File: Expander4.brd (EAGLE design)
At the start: 160 x 100 mm, 6 parts, among them K1 G5L, K2 G5L, K3 G5L, K4 G5L

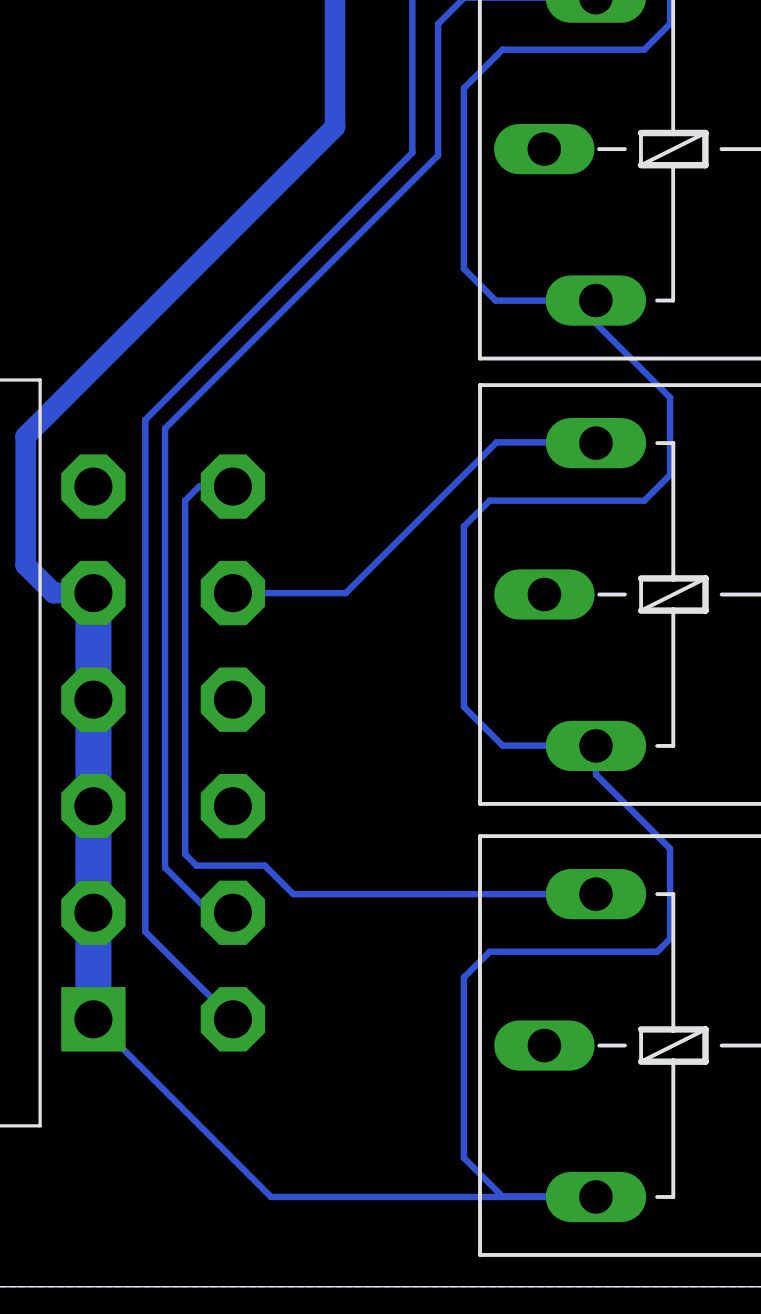
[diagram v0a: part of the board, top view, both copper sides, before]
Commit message: Protective diodes added in expander
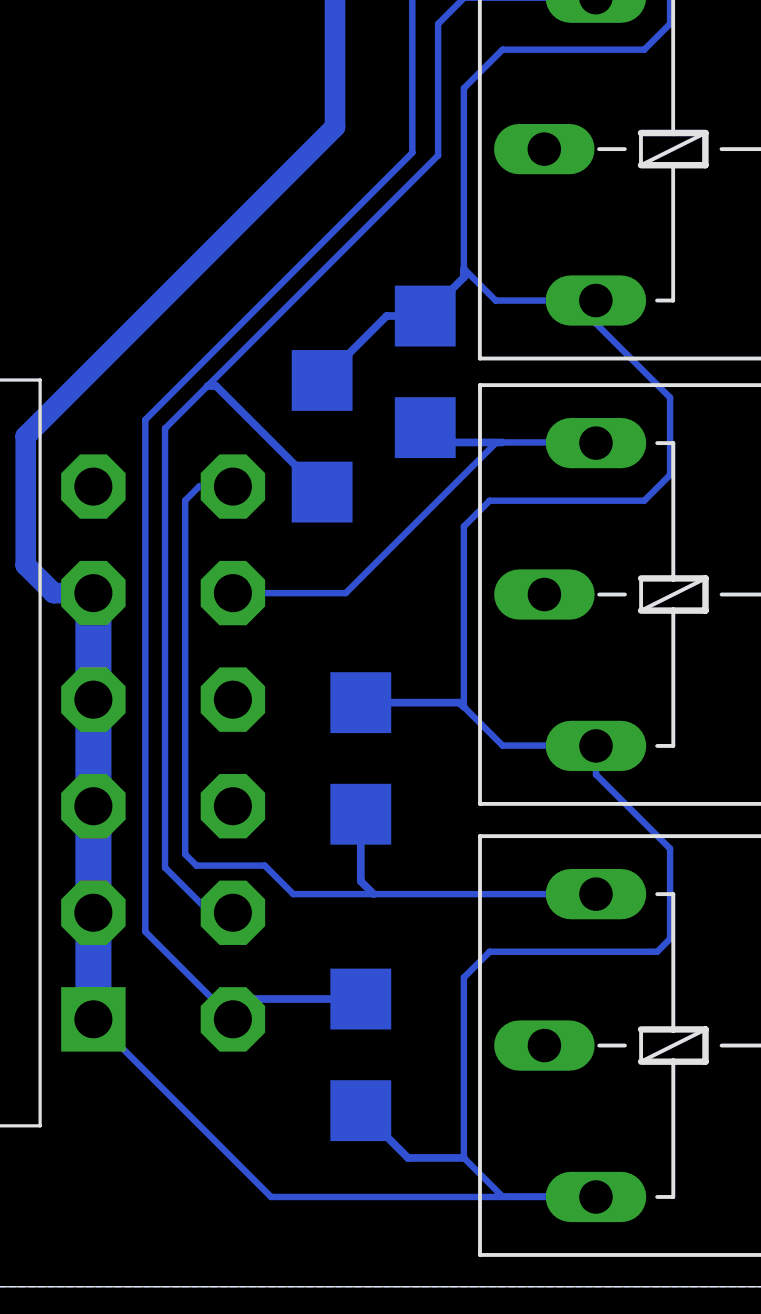
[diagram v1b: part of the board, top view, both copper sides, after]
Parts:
- added D1, D2, D3, D4: (no value), SparkFun-DiscreteSemi:SMB-DIODE
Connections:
- net 12V: now also D1.C, D2.C, D3.C, D4.C
- net L1: now also D2.A
- net L2: now also D1.A
- net L3: now also D3.A
- net L4: now also D4.A
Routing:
- net 12V: track 255.9 -> 272.5 mm
- net L3: track 47.8 -> 54.0 mm
- net L4: track 66.8 -> 72.2 mm
- net L1: track 32.9 -> 36.3 mm
- net L2: track 16.8 -> 20.1 mm
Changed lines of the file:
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@@
 </element>
 <element name="OUT" library="con-amphenol" package="MF42-10" value="MF42-10" x="53.634" y="14.738" rot="R90"/>
+<element name="D1" library="SparkFun-DiscreteSemi" package="SMB-DIODE" value="" x="18.796" y="36.068" rot="MR270"/>
+<element name="D2" library="SparkFun-DiscreteSemi" package="SMB-DIODE" value="" x="16.256" y="20.828" rot="MR270"/>
+<element name="D3" library="SparkFun-DiscreteSemi" package="SMB-DIODE" value="" x="14.732" y="33.528" rot="MR270"/>
+<element name="D4" library="SparkFun-DiscreteSemi" package="SMB-DIODE" value="" x="16.256" y="9.144" rot="MR90"/>
 </elements>
 <signals>
@@
 <wire x1="4.151" y1="27.345" x2="5.715" y2="27.345" width="0.8128" layer="16"/>
 <wire x1="28.448" y1="71.12" x2="23.876" y2="71.12" width="0.8128" layer="16"/>
+<contactref element="D1" pad="C"/>
+<contactref element="D2" pad="C"/>
+<contactref element="D3" pad="C"/>
+<contactref element="D4" pad="C"/>
+<wire x1="14.732" y1="35.728" x2="17.272" y2="38.268" width="0.3048" layer="16"/>
+<wire x1="17.272" y1="38.268" x2="18.796" y2="38.268" width="0.3048" layer="16"/>
+<wire x1="18.796" y1="38.268" x2="20.32" y2="39.792" width="0.3048" layer="16"/>
+<wire x1="20.32" y1="39.792" x2="20.32" y2="40.132" width="0.3048" layer="16"/>
+<wire x1="16.256" y1="23.028" x2="20.152" y2="23.028" width="0.3048" layer="16"/>
+<wire x1="20.152" y1="23.028" x2="20.32" y2="22.86" width="0.3048" layer="16"/>
+<wire x1="20.32" y1="5.08" x2="18.12" y2="5.08" width="0.3048" layer="16"/>
+<wire x1="18.12" y1="5.08" x2="16.256" y2="6.944" width="0.3048" layer="16"/>
 </signal>
 <signal name="GND">
@@
 <contactref element="IN" pad="12"/>
 <contactref element="K1" pad="2"/>
-<wire x1="25.527" y1="15.479" x2="13.59638125" y2="15.479" width="0.254" layer="16"/>
+<wire x1="25.527" y1="15.479" x2="16.764" y2="15.479" width="0.254" layer="16"/>
+<wire x1="16.764" y1="15.479" x2="13.59638125" y2="15.479" width="0.254" layer="16"/>
 <wire x1="13.59638125" y1="15.479" x2="12.4714" y2="16.60398125" width="0.254" layer="16"/>
 <wire x1="12.4714" y1="16.60398125" x2="9.778996875" y2="16.60398125" width="0.254" layer="16"/>
@@
 <wire x1="9.331959375" y1="30.99561875" x2="9.881340625" y2="31.545" width="0.254" layer="16"/>
 <wire x1="9.881340625" y1="31.545" x2="11.215" y2="31.545" width="0.254" layer="16"/>
+<contactref element="D2" pad="A"/>
+<wire x1="16.256" y1="18.628" x2="16.256" y2="15.987" width="0.3048" layer="16"/>
+<wire x1="16.256" y1="15.987" x2="16.764" y2="15.479" width="0.3048" layer="16"/>
 </signal>
 <signal name="L2">
 <contactref element="IN" pad="11"/>
 <contactref element="K2" pad="2"/>
-<wire x1="21.600159375" y1="33.284159375" x2="25.501840625" y2="33.284159375" width="0.254" layer="16"/>
+<wire x1="21.600159375" y1="33.284159375" x2="21.844" y2="33.284159375" width="0.254" layer="16"/>
+<wire x1="21.844" y1="33.284159375" x2="25.501840625" y2="33.284159375" width="0.254" layer="16"/>
 <wire x1="25.501840625" y1="33.284159375" x2="25.527" y2="33.259" width="0.254" layer="16"/>
 <wire x1="21.600159375" y1="33.284159375" x2="15.661" y2="27.345" width="0.254" layer="16"/>
 <wire x1="15.661" y1="27.345" x2="11.215" y2="27.345" width="0.254" layer="16"/>
+<contactref element="D1" pad="A"/>
+<wire x1="18.796" y1="33.868" x2="19.379840625" y2="33.284159375" width="0.3048" layer="16"/>
+<wire x1="19.379840625" y1="33.284159375" x2="21.844" y2="33.284159375" width="0.3048" layer="16"/>
 </signal>
 <signal name="L3">
@@
 <wire x1="8.53948125" y1="33.83448125" x2="8.53948125" y2="16.5227" width="0.254" layer="16"/>
 <wire x1="20.337" y1="50.817" x2="25.522" y2="50.817" width="0.254" layer="16"/>
-<wire x1="8.53948125" y1="33.83448125" x2="19.304" y2="44.599" width="0.254" layer="16"/>
+<wire x1="8.53948125" y1="33.83448125" x2="10.2125" y2="35.5075" width="0.254" layer="16"/>
+<wire x1="10.2125" y1="35.5075" x2="19.304" y2="44.599" width="0.254" layer="16"/>
 <wire x1="19.304" y1="44.599" x2="19.304" y2="49.784" width="0.254" layer="16"/>
 <wire x1="19.304" y1="49.784" x2="20.337" y2="50.817" width="0.254" layer="16"/>
+<contactref element="D3" pad="A"/>
+<wire x1="14.732" y1="31.328" x2="10.5525" y2="35.5075" width="0.3048" layer="16"/>
+<wire x1="10.5525" y1="35.5075" x2="10.2125" y2="35.5075" width="0.3048" layer="16"/>
 </signal>
 <signal name="L4">
@@
 <wire x1="18.288" y1="61.468" x2="25.321" y2="68.501" width="0.254" layer="16"/>
 <wire x1="25.321" y1="68.501" x2="25.501" y2="68.501" width="0.254" layer="16"/>
+<contactref element="D4" pad="A"/>
+<wire x1="16.256" y1="11.344" x2="12.014" y2="11.344" width="0.3048" layer="16"/>
+<wire x1="12.014" y1="11.344" x2="11.215" y2="10.545" width="0.3048" layer="16"/>
 </signal>
 <signal name="O1">
